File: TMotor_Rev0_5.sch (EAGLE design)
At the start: 83 parts, among them U1 INA125U, U10 DEV-16771, U2 INA125U, U3 INA125U, U4 INA125U, U5 SN65HVD230MDREP

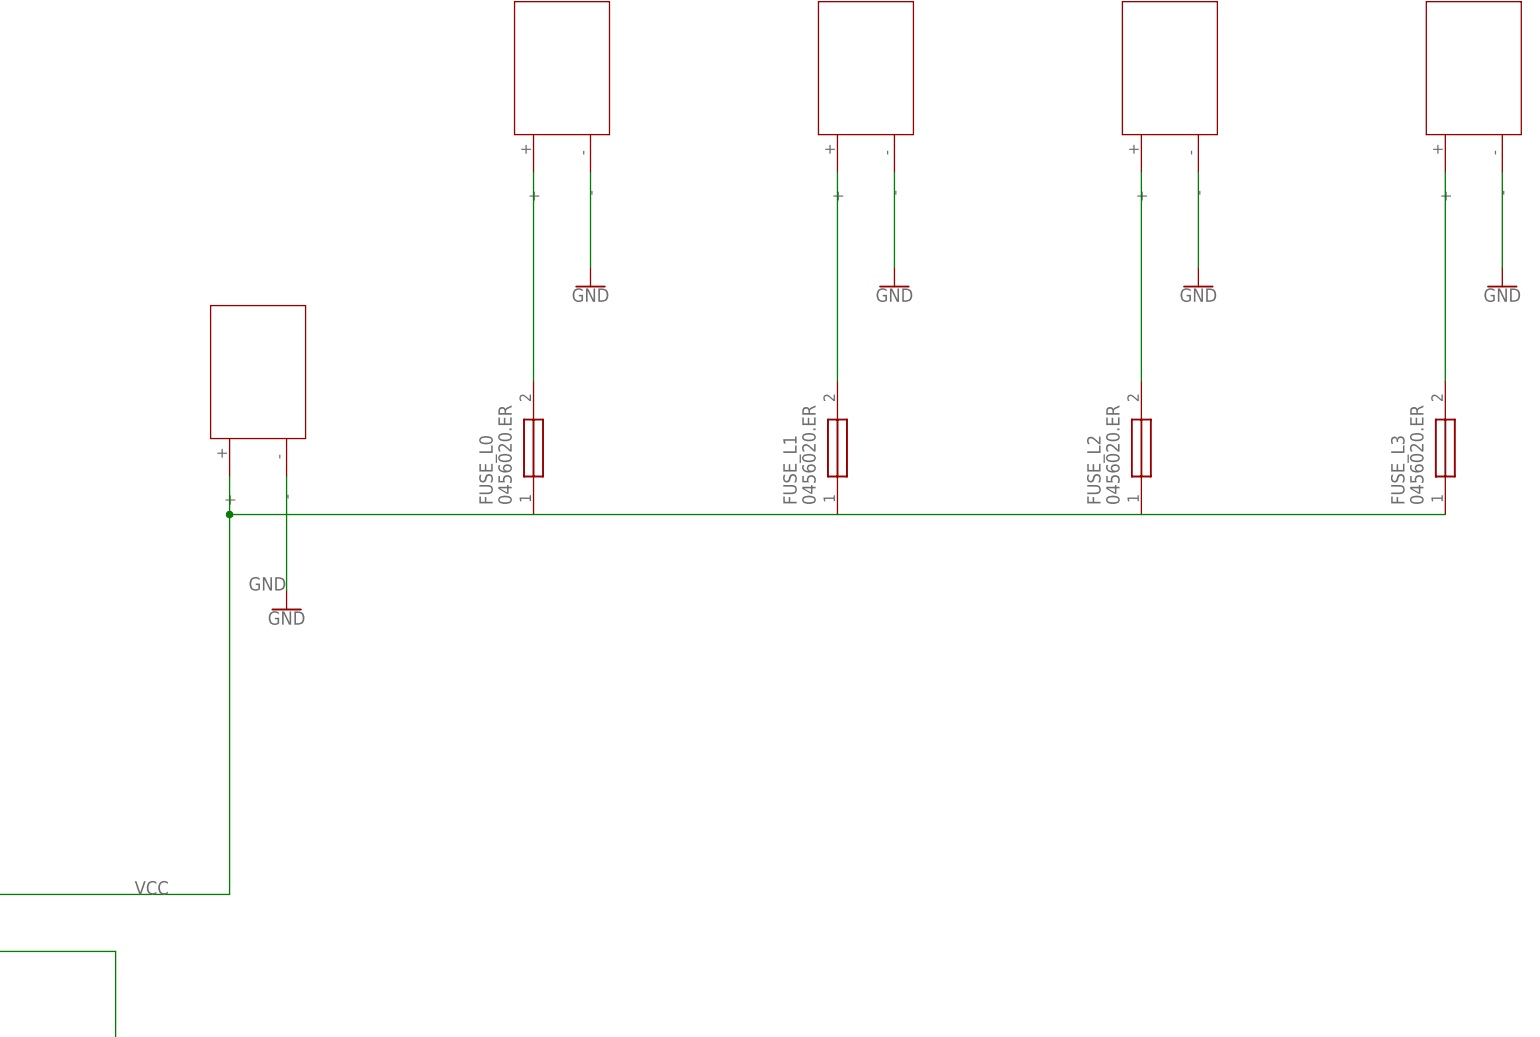
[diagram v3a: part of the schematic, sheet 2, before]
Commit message: Arranged new connectors
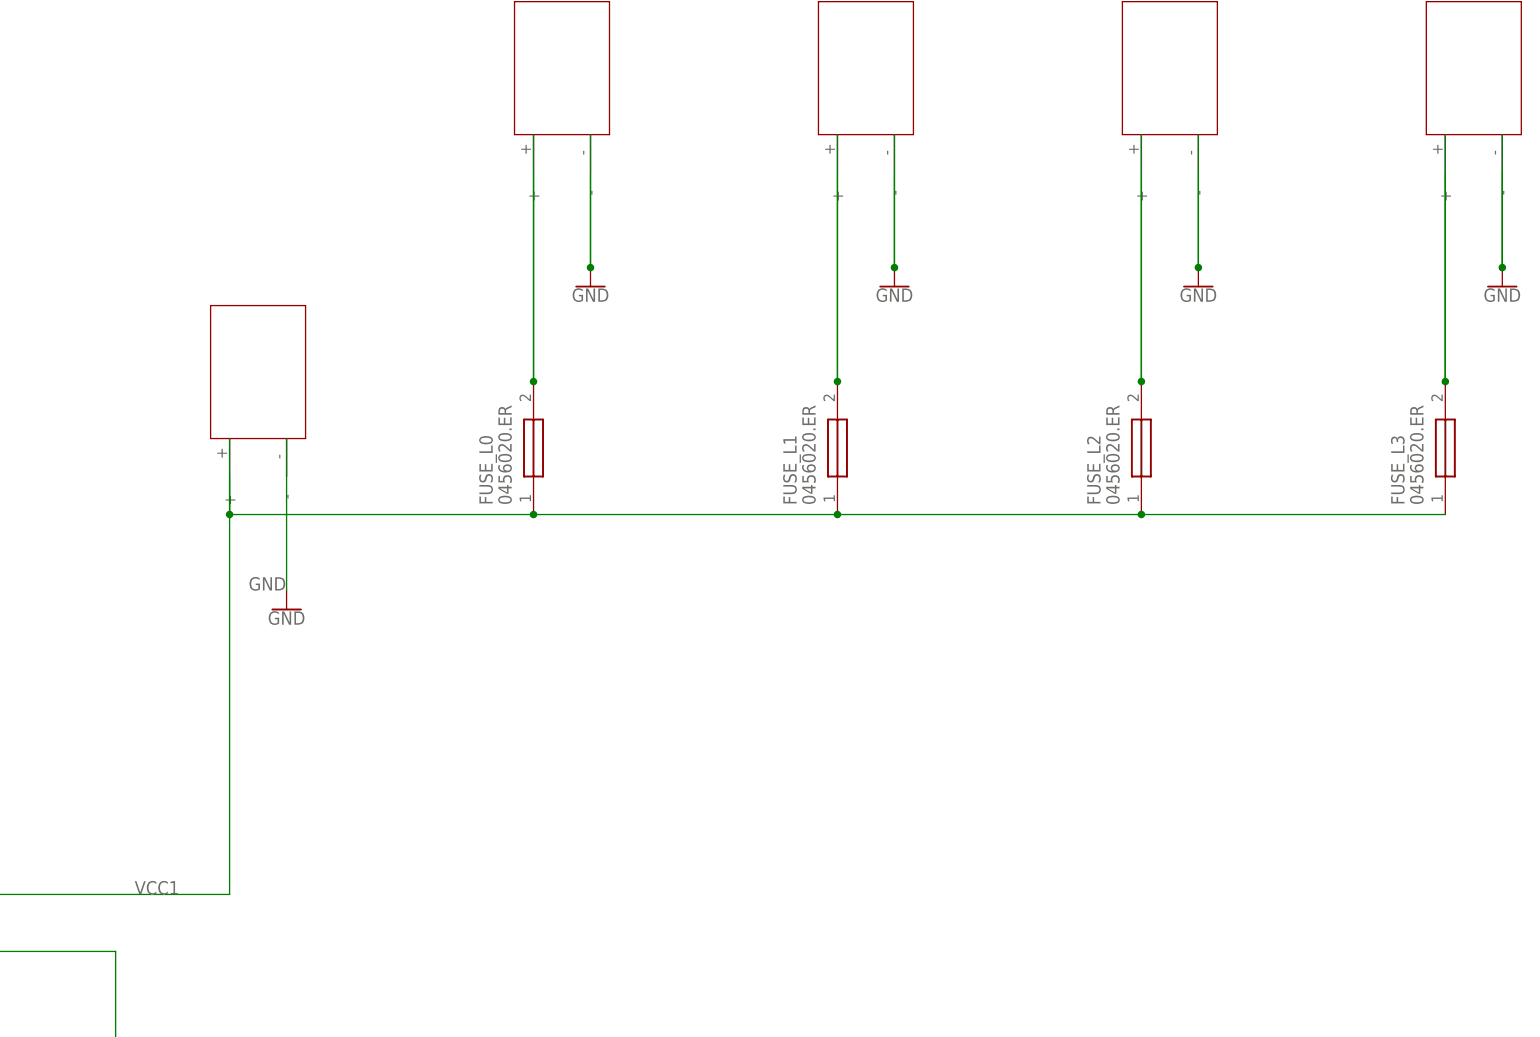
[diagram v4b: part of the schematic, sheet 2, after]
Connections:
- removed net VCC: FUSE_L0.1, R2.2, SHUNT.2
- removed net VCC2: FUSE_L2.1
- removed net VCC3: FUSE_L3.1
- net GND: now also XT30UPB-F.-, XT30UPB-F1.-, XT30UPB-F2.-, XT30UPB-F3.-, XT30UPB-F4.-
- net N$43: now also XT30UPB-F1.+
- net N$46: now also XT30UPB-F2.+
- net N$47: now also XT30UPB-F3.+
- net N$53: now also XT30UPB-F.+
- net VCC1: now also FUSE_L0.1, FUSE_L2.1, FUSE_L3.1, R2.2, SHUNT.2, XT30UPB-F4.+
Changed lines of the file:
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@@
 <segment>
 <pinref part="GND5" gate="1" pin="GND"/>
-<wire x1="-68.58" y1="243.84" x2="-68.58" y2="259.08" width="0.1524" layer="91"/>
 <label x="-73.66" y="243.84" size="1.778" layer="95"/>
+<pinref part="XT30UPB-F4" gate="G$1" pin="-"/>
+<wire x1="-68.58" y1="243.84" x2="-68.58" y2="264.16" width="0.1524" layer="91"/>
 </segment>
 <segment>
@@
 <pinref part="GND8" gate="1" pin="GND"/>
 <wire x1="-27.94" y1="299.72" x2="-27.94" y2="287.02" width="0.1524" layer="91"/>
+<pinref part="XT30UPB-F" gate="G$1" pin="-"/>
+<wire x1="-27.94" y1="304.8" x2="-27.94" y2="287.02" width="0.1524" layer="91"/>
+<junction x="-27.94" y="287.02"/>
 </segment>
 <segment>
 <pinref part="GND9" gate="1" pin="GND"/>
 <wire x1="12.7" y1="299.72" x2="12.7" y2="287.02" width="0.1524" layer="91"/>
+<pinref part="XT30UPB-F1" gate="G$1" pin="-"/>
+<wire x1="12.7" y1="304.8" x2="12.7" y2="287.02" width="0.1524" layer="91"/>
+<junction x="12.7" y="287.02"/>
 </segment>
 <segment>
 <pinref part="GND24" gate="1" pin="GND"/>
 <wire x1="53.34" y1="299.72" x2="53.34" y2="287.02" width="0.1524" layer="91"/>
+<pinref part="XT30UPB-F2" gate="G$1" pin="-"/>
+<wire x1="53.34" y1="304.8" x2="53.34" y2="287.02" width="0.1524" layer="91"/>
+<junction x="53.34" y="287.02"/>
 </segment>
 <segment>
 <pinref part="GND25" gate="1" pin="GND"/>
 <wire x1="93.98" y1="299.72" x2="93.98" y2="287.02" width="0.1524" layer="91"/>
+<pinref part="XT30UPB-F3" gate="G$1" pin="-"/>
+<wire x1="93.98" y1="304.8" x2="93.98" y2="287.02" width="0.1524" layer="91"/>
+<junction x="93.98" y="287.02"/>
 </segment>
 </net>
@@
 <label x="-256.54" y="99.06" size="1.778" layer="95"/>
 <junction x="-256.54" y="99.06"/>
-</segment>
-</net>
-<net name="VCC" class="0">
-<segment>
-<wire x1="-76.2" y1="203.2" x2="-144.78" y2="203.2" width="0.1524" layer="91"/>
-<label x="-88.9" y="203.2" size="1.778" layer="95"/>
-<wire x1="-76.2" y1="203.2" x2="-76.2" y2="254" width="0.1524" layer="91"/>
-<wire x1="-76.2" y1="254" x2="-76.2" y2="259.08" width="0.1524" layer="91"/>
-<wire x1="-76.2" y1="254" x2="-35.56" y2="254" width="0.1524" layer="91"/>
-<junction x="-76.2" y="254"/>
-<pinref part="FUSE_L0" gate="G$1" pin="1"/>
-<wire x1="-144.78" y1="203.2" x2="-144.78" y2="218.44" width="0.1524" layer="91"/>
-<pinref part="SHUNT" gate="A" pin="2"/>
-<junction x="-144.78" y="203.2"/>
-<pinref part="R2" gate="G$1" pin="2"/>
-<wire x1="-144.78" y1="218.44" x2="-147.32" y2="218.44" width="0.1524" layer="91"/>
 </segment>
 </net>
@@
 <pinref part="FUSE_L0" gate="G$1" pin="2"/>
 <wire x1="-35.56" y1="271.78" x2="-35.56" y2="299.72" width="0.1524" layer="91"/>
+<pinref part="XT30UPB-F" gate="G$1" pin="+"/>
+<wire x1="-35.56" y1="304.8" x2="-35.56" y2="271.78" width="0.1524" layer="91"/>
+<junction x="-35.56" y="271.78"/>
 </segment>
 </net>
@@
 <net name="VCC1" class="0">
 <segment>
+<wire x1="-76.2" y1="203.2" x2="-144.78" y2="203.2" width="0.1524" layer="91"/>
+<label x="-88.9" y="203.2" size="1.778" layer="95"/>
+<wire x1="-76.2" y1="203.2" x2="-76.2" y2="254" width="0.1524" layer="91"/>
+<wire x1="-76.2" y1="254" x2="-76.2" y2="259.08" width="0.1524" layer="91"/>
+<wire x1="-144.78" y1="203.2" x2="-144.78" y2="218.44" width="0.1524" layer="91"/>
+<pinref part="SHUNT" gate="A" pin="2"/>
+<junction x="-144.78" y="203.2"/>
+<pinref part="R2" gate="G$1" pin="2"/>
+<wire x1="-144.78" y1="218.44" x2="-147.32" y2="218.44" width="0.1524" layer="91"/>
+<pinref part="FUSE_L0" gate="G$1" pin="1"/>
+<wire x1="-76.2" y1="254" x2="-35.56" y2="254" width="0.1524" layer="91"/>
+<junction x="-76.2" y="254"/>
+<pinref part="FUSE_L1" gate="G$1" pin="1"/>
 <wire x1="-35.56" y1="254" x2="5.08" y2="254" width="0.1524" layer="91"/>
-<pinref part="FUSE_L1" gate="G$1" pin="1"/>
+<junction x="-35.56" y="254"/>
+<pinref part="FUSE_L2" gate="G$1" pin="1"/>
+<wire x1="5.08" y1="254" x2="45.72" y2="254" width="0.1524" layer="91"/>
+<junction x="5.08" y="254"/>
+<pinref part="FUSE_L3" gate="G$1" pin="1"/>
+<wire x1="45.72" y1="254" x2="86.36" y2="254" width="0.1524" layer="91"/>
+<junction x="45.72" y="254"/>
+<pinref part="XT30UPB-F4" gate="G$1" pin="+"/>
+<wire x1="-76.2" y1="254" x2="-76.2" y2="264.16" width="0.1524" layer="91"/>
 </segment>
 </net>
@@
 <pinref part="FUSE_L1" gate="G$1" pin="2"/>
 <wire x1="5.08" y1="271.78" x2="5.08" y2="299.72" width="0.1524" layer="91"/>
-</segment>
-</net>
-<net name="VCC2" class="0">
-<segment>
-<wire x1="5.08" y1="254" x2="45.72" y2="254" width="0.1524" layer="91"/>
-<pinref part="FUSE_L2" gate="G$1" pin="1"/>
+<pinref part="XT30UPB-F1" gate="G$1" pin="+"/>
+<wire x1="5.08" y1="304.8" x2="5.08" y2="271.78" width="0.1524" layer="91"/>
+<junction x="5.08" y="271.78"/>
 </segment>
 </net>
@@
 <pinref part="FUSE_L2" gate="G$1" pin="2"/>
 <wire x1="45.72" y1="271.78" x2="45.72" y2="299.72" width="0.1524" layer="91"/>
-</segment>
-</net>
-<net name="VCC3" class="0">
-<segment>
-<wire x1="45.72" y1="254" x2="86.36" y2="254" width="0.1524" layer="91"/>
-<pinref part="FUSE_L3" gate="G$1" pin="1"/>
+<pinref part="XT30UPB-F2" gate="G$1" pin="+"/>
+<wire x1="45.72" y1="304.8" x2="45.72" y2="271.78" width="0.1524" layer="91"/>
+<junction x="45.72" y="271.78"/>
 </segment>
 </net>
@@
 <pinref part="FUSE_L3" gate="G$1" pin="2"/>
 <wire x1="86.36" y1="271.78" x2="86.36" y2="299.72" width="0.1524" layer="91"/>
-</segment>
-</net>
+<pinref part="XT30UPB-F3" gate="G$1" pin="+"/>
+<wire x1="86.36" y1="304.8" x2="86.36" y2="271.78" width="0.1524" layer="91"/>
+<junction x="86.36" y="271.78"/>
+</segment>
+</net>

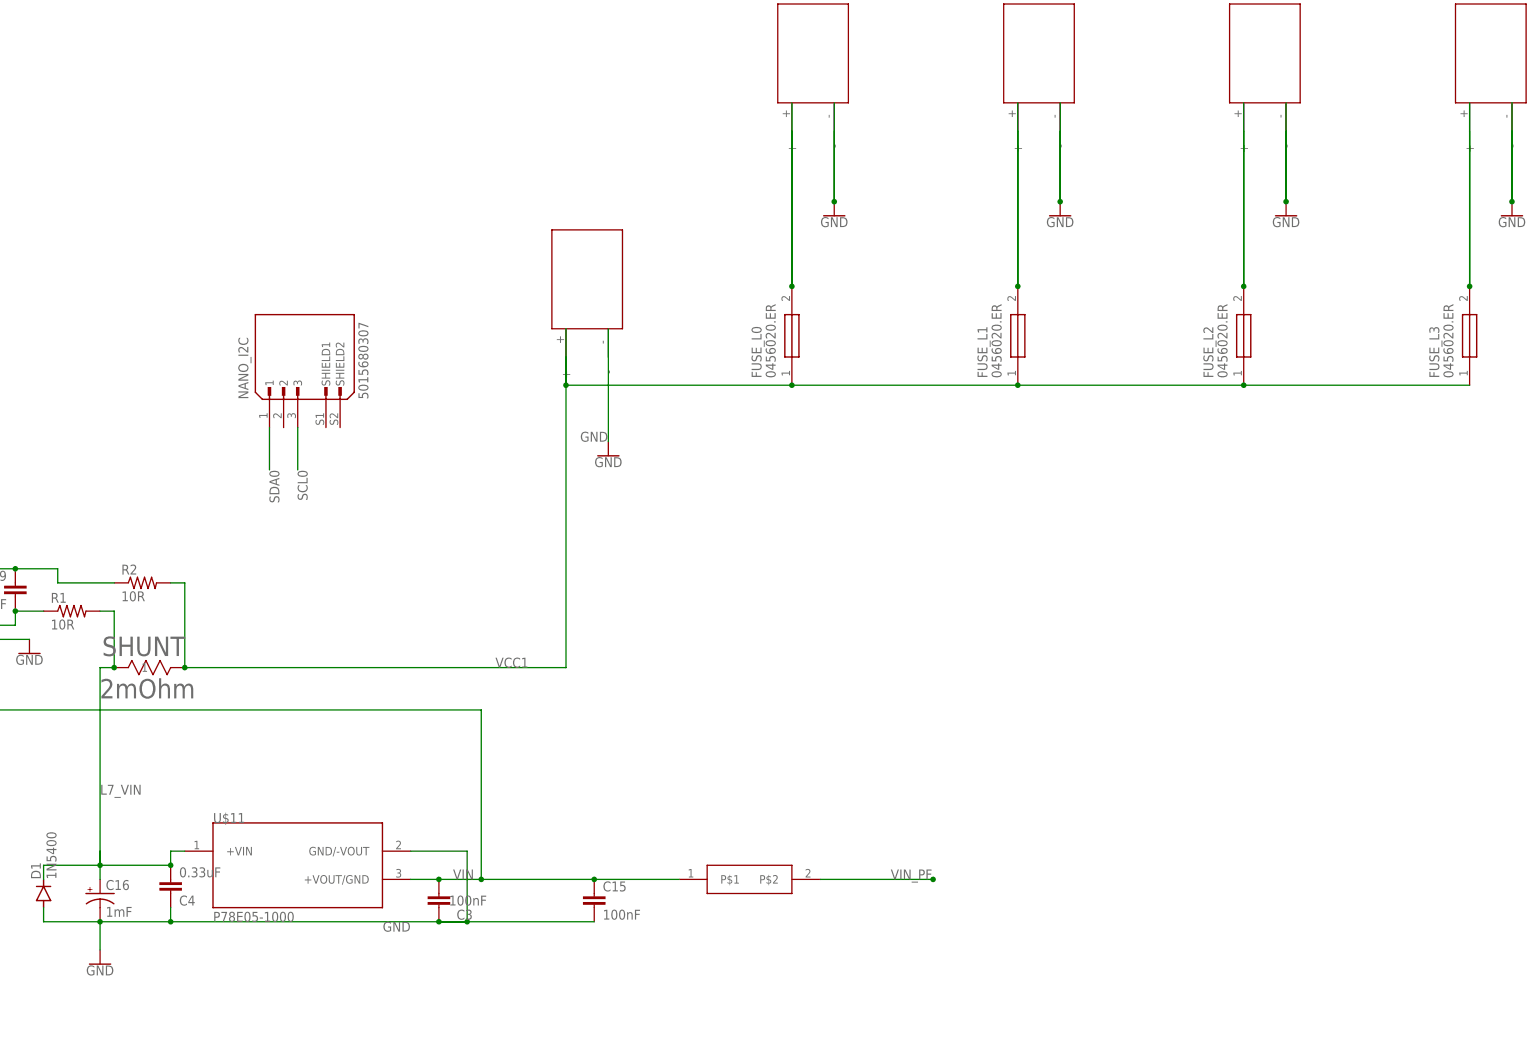
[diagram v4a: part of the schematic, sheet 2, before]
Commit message: Signed-off-by: NAU\cfc65 <chancecuddeback@gmail.com>
Passed DRC check. Need to perform a more rigorous manual review.
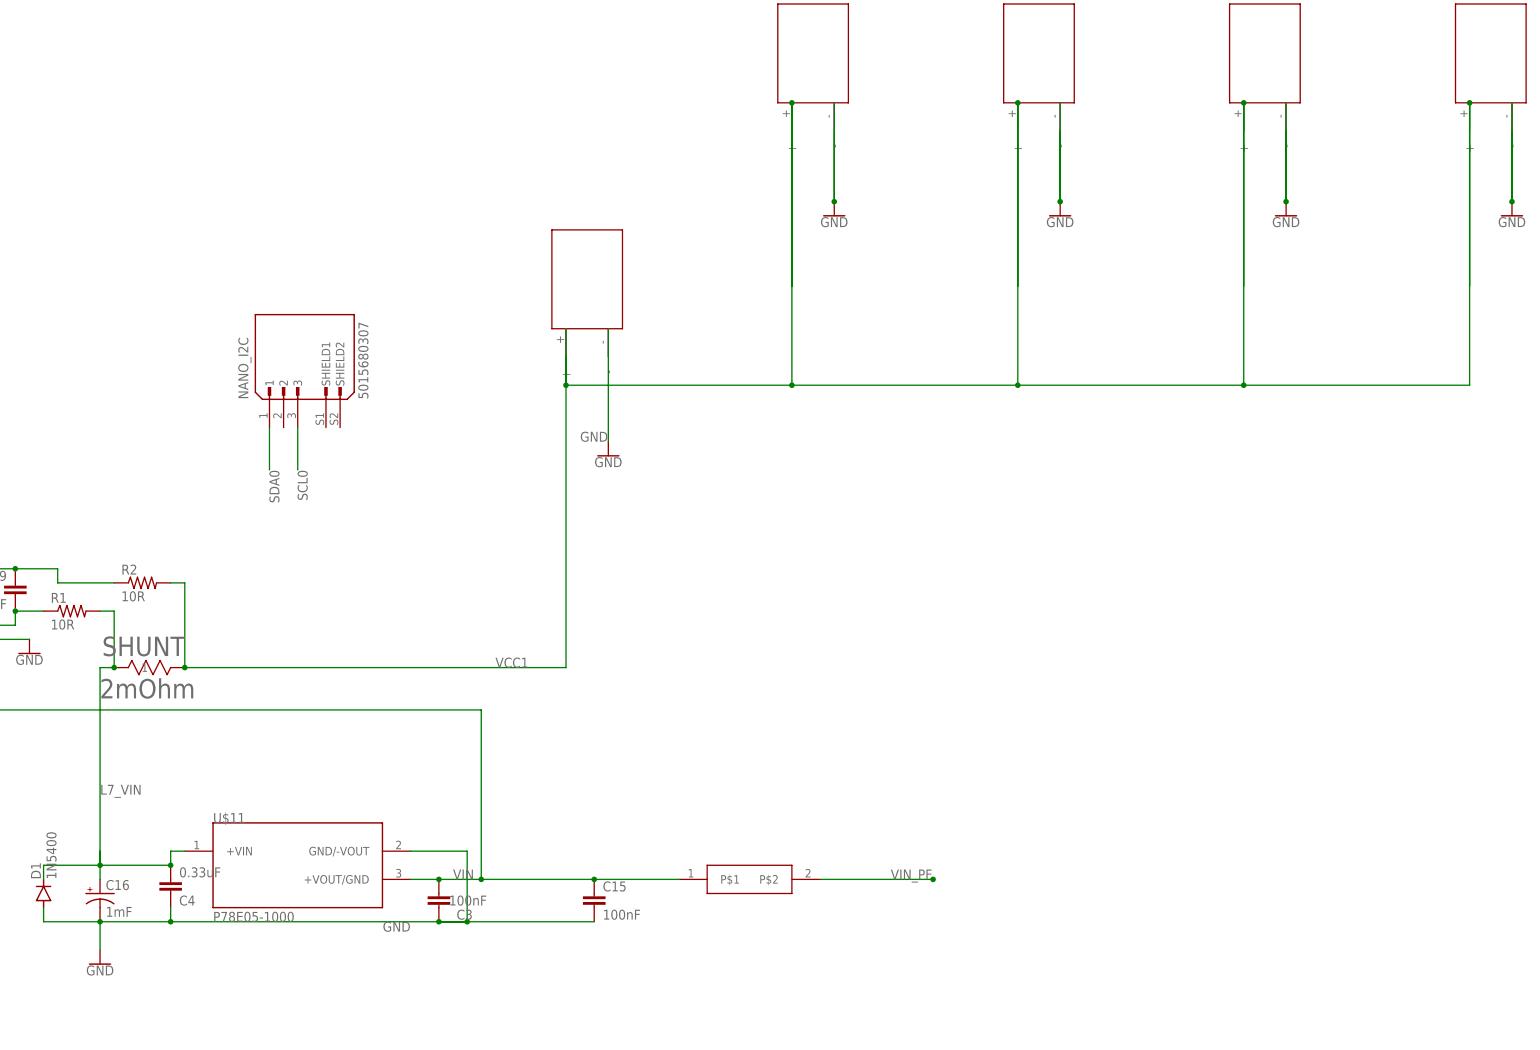
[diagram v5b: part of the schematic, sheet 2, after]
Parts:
- removed FUSE_L0, FUSE_L1, FUSE_L2, FUSE_L3: 0456020.ER, SamacSys_Parts:0456020.ER
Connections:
- removed net N$43: FUSE_L1.2, XT30UPB-F1.+
- removed net N$46: FUSE_L2.2, XT30UPB-F2.+
- removed net N$47: FUSE_L3.2, XT30UPB-F3.+
- removed net N$53: FUSE_L0.2, XT30UPB-F.+
- removed net SCK: U10.SCK
- net STOP: now also U10.OUT1C
- net VCC1: now also XT30UPB-F.+, XT30UPB-F1.+, XT30UPB-F2.+, XT30UPB-F3.+; no longer FUSE_L0.1, FUSE_L1.1, FUSE_L2.1, FUSE_L3.1

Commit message: Post review
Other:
- moved on the sheet: NANO_I2C
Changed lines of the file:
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@@
 </instance>
 <instance part="U$6" gate="G$1" x="-43.18" y="165.1" smashed="yes"/>
-<instance part="NANO_I2C" gate="G$1" x="-124.46" y="259.08" smashed="yes" rot="R90">
-<attribute name="NAME" x="-133.35" y="251.46" size="1.778" layer="95" rot="R90"/>
-<attribute name="VALUE" x="-111.76" y="251.46" size="1.778" layer="96" rot="R90"/>
+<instance part="NANO_I2C" gate="G$1" x="-299.72" y="271.78" smashed="yes" rot="R180">
+<attribute name="NAME" x="-292.1" y="262.89" size="1.778" layer="95" rot="R180"/>
+<attribute name="VALUE" x="-292.1" y="284.48" size="1.778" layer="96" rot="R180"/>
 </instance>
 <instance part="U$11" gate="G$1" x="-124.46" y="167.64" smashed="yes">
@@
 <segment>
 <pinref part="NANO_I2C" gate="G$1" pin="1"/>
-<wire x1="-129.54" y1="246.38" x2="-129.54" y2="238.76" width="0.1524" layer="91"/>
-<label x="-129.54" y="238.76" size="1.778" layer="95" rot="R270"/>
+<wire x1="-287.02" y1="266.7" x2="-279.4" y2="266.7" width="0.1524" layer="91"/>
+<label x="-279.4" y="266.7" size="1.778" layer="95" rot="R270"/>
 </segment>
 </net>
@@
 <segment>
 <pinref part="NANO_I2C" gate="G$1" pin="3"/>
-<wire x1="-124.46" y1="246.38" x2="-124.46" y2="238.76" width="0.1524" layer="91"/>
-<label x="-124.46" y="238.76" size="1.778" layer="95" rot="R270"/>
-</segment>
-</net>
+<wire x1="-287.02" y1="271.78" x2="-279.4" y2="271.78" width="0.1524" layer="91"/>
+<label x="-279.4" y="276.86" size="1.778" layer="95" rot="R270"/>
+</segment>
+</net>
